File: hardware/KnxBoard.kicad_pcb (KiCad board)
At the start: 4 copper layers, 41.8 x 41.9 mm, 47 parts, among them IC0 STM32G491KEU6, IC1 NCN5130, J1 Conn_01x16, J2 Conn_01x16, J4 Conn_01x02_Male, X1 FA-238

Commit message: Routage OK need check and mass and texts
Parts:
- removed C1 (x2): 100 nF, Capacitor_SMD:C_0603_1608Metric_Pad1.08x0.95mm_HandSolder
- removed the C11 at (113.3, 55.4)
- removed C5_9: 100nF, Capacitor_SMD:C_0603_1608Metric_Pad1.08x0.95mm_HandSolder
- removed JP0, JP5: Bootloader, Jumper:SolderJumper-2_P1.3mm_Open_TrianglePad1.0x1.5mm
- added C20: 100 nF, Capacitor_SMD:C_0603_1608Metric_Pad1.08x0.95mm_HandSolder, F.Cu at (114.6, 36.1)
- added C8: 100nF 50V, Capacitor_SMD:C_0603_1608Metric_Pad1.08x0.95mm_HandSolder, F.Cu at (106.9, 61.2)
- added C9: 100uF 35V, Capacitor_SMD:CP_Elec_6.3x7.7, F.Cu at (92.2, 65.8)
- added JP3: Speed, Jumper:SolderJumper-3_P1.3mm_Open_RoundedPad1.0x1.5mm, B.Cu at (106.4, 49.0)
- added TP1: KNX_RXD, TestPoint:TestPoint_Pad_D1.0mm, F.Cu at (101.6, 50.0)
- added TP2: KNX_TXD, TestPoint:TestPoint_Pad_D1.0mm, F.Cu at (107.4, 47.8)
- C10: renamed from C12; value 1uF 35V ESR < 2ohm -> 1uF 50V ESR < 2ohm; moved to F.Cu
- C11: renamed from C19; moved to F.Cu
- C12: renamed from C20; moved to F.Cu
- C16, C17, C4: moved to F.Cu
- C21: renamed from C5; moved to F.Cu
- C22: renamed from C3; moved to F.Cu
- C23: renamed from C2; moved to F.Cu
- C24: renamed from C4; moved to F.Cu
- C3: renamed from C15; moved to F.Cu
- C4: renamed from C6; moved to F.Cu
- C5: renamed from C14; moved to F.Cu
- C6: renamed from C13; moved to F.Cu
- C7: renamed from C10; moved to F.Cu
- D1: value SS16 -> SS16T3G
- J1, J2: value Conn_01x16 -> Conn_01x15; footprint Connector_PinHeader_2.54mm:PinHeader_1x16_P2.54mm_Vertical -> Connector_PinHeader_2.54mm:PinHeader_1x15_P2.54mm_Vertical
- J4: value Conn_01x02_Male -> Conn_01x02
- JP1: value Bootflash -> Clock_8_16; footprint Jumper:SolderJumper-2_P1.3mm_Open_TrianglePad1.0x1.5mm -> Jumper:SolderJumper-3_P1.3mm_Open_RoundedPad1.0x1.5mm
- JP2: value RESETB_NRST -> Parity; footprint Jumper:SolderJumper-2_P1.3mm_Open_TrianglePad1.0x1.5mm -> Jumper:SolderJumper-3_P1.3mm_Open_RoundedPad1.0x1.5mm
- JP4: value Bootflash -> BootMode; footprint Jumper:SolderJumper-2_P1.3mm_Open_TrianglePad1.0x1.5mm -> Jumper:SolderJumper-3_P1.3mm_Open_RoundedPad1.0x1.5mm
- R22: renamed from R3; moved to F.Cu
- R3: renamed from R1; moved to B.Cu
- moved C11 21.5 mm to (113.3, 64.0), turned to 0 degrees
- moved JP4 21.0 mm to (112.5, 49.0), turned to 90 degrees
- moved R10 17.3 mm to (97.5, 65.3), turned to 0 degrees
- moved R18 16.4 mm to (109.7, 61.0), turned to -90 degrees
- moved C3 16.4 mm to (96.9, 61.7), turned to 0 degrees
- moved JP2 15.5 mm to (102.9, 49.0), turned to 90 degrees
- moved L2 15.1 mm to (109.2, 56.9)
- moved C4 14.1 mm to (97.5, 50.8), turned to -90 degrees
- moved R3 13.0 mm to (97.5, 65.0), turned to -90 degrees
- moved R21 12.5 mm to (113.8, 53.1), turned to 90 degrees
- moved JP1 12.3 mm to (99.6, 49.0), turned to 90 degrees
- moved C10 11.2 mm to (106.2, 64.0), turned to -90 degrees
- moved LD1 11.1 mm to (92.5, 49.3), turned to 180 degrees
- moved R30 11.1 mm to (92.5, 47.5)
- moved D1 10.9 mm to (109.2, 66.3)
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- renumbered C18 to C30, JP3 to JP7, L1 to L2, L2 to L3, R6 to R10, R2 to R18, R4 to R20, R5 to R21, R21 to R30
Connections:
- C10 pad 1: /KNXIFACE/Vfilt -> Net-(C10-Pad1)
- C4 pad 1: VDD -> +3V3
- D2 pad 1: /KNXIFACE/KNX+ -> GNDREF
- D2 pad 2: GNDREF -> /KNXIFACE/KNX+
- IC0 pad 19: KNX_RXD -> /KNXIFACE/KNX_RXD
- IC0 pad 20: KNX_TXD -> /KNXIFACE/KNX_TXD
- IC1 pad 10: /KNXIFACE/Vfilt -> Net-(C10-Pad1)
- IC1 pad 26: GNDREF -> Net-(IC1-Pad26)
- IC1 pad 27: KNX_RXD -> /KNXIFACE/KNX_RXD
- IC1 pad 28: KNX_TXD -> /KNXIFACE/KNX_TXD
- IC1 pad 29: GNDREF -> Net-(IC1-Pad29)
- IC1 pad 33: GNDREF -> Net-(JP1-Pad2)
- J1 pad 1: Prog -> +12V
- J1 pad 10: /MCU/PB4 -> /MCU/PB5
- J1 pad 11: /MCU/PB5 -> /MCU/PB6
- J1 pad 12: /MCU/PB6 -> /MCU/PB7
- J1 pad 13: /MCU/PB7 -> /MCU/PB8
- J1 pad 14: /MCU/PB8 -> VDD
- J1 pad 15: VDD -> GNDREF
- J1 pad 2: KNX_TXD -> GNDREF
- J1 pad 3: KNX_RXD -> unconnected-(J1-Pad3)
- J1 pad 4: KNX_RESETB -> NRST
- J1 pad 5: KNX_SAVEB -> /MCU/DEBUG_JTMS-SWDIO
- J1 pad 6: /MCU/DEBUG_JTMS-SWDIO -> /MCU/DEBUG_JTCK-SWCLK
- J1 pad 7: /MCU/DEBUG_JTCK-SWCLK -> /MCU/DEBUG_JTDI
- J1 pad 8: /MCU/DEBUG_JTDI -> /MCU/DEBUG_JTDA-SWO
- J1 pad 9: /MCU/DEBUG_JTDA-SWO -> /MCU/PB4
- J2 pad 1: +12V -> unconnected-(J2-Pad1)
- J2 pad 14: NRST -> /MCU/PF1
- J2 pad 15: /MCU/PF1 -> CLK16
- J2 pad 4: GNDREF -> Prog
- J4 pad 1: /KNXIFACE/KNX+ -> GNDREF
- J4 pad 2: GNDREF -> /KNXIFACE/KNX+
- JP1 pad 2: Net-(JP0-Pad1) -> Net-(JP1-Pad2)
- JP2 pad 1: NRST -> GNDREF
- JP2 pad 2: KNX_RESETB -> Net-(IC1-Pad29)
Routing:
- net GNDREF: track 0.00 -> 264.3 mm, vias 0 -> 34
- net VDD: track 0.00 -> 98.8 mm, vias 0 -> 4
- net Prog: track 0.00 -> 66.0 mm, vias 0 -> 2
- net CLK16: track 0.00 -> 65.1 mm, vias 0 -> 1
- net NRST: track 0.00 -> 53.9 mm, vias 0 -> 5
- net +3V3: track 0.00 -> 51.8 mm, vias 0 -> 4
- net /MCU/PA7: track 0.00 -> 33.5 mm, vias 0 -> 2
- net KNX_RESETB: track 0.00 -> 33.0 mm, vias 0 -> 2
- net /MCU/PA6: track 0.00 -> 32.5 mm, vias 0 -> 1
- net KNX_SAVEB: track 0.00 -> 32.0 mm, vias 0 -> 2
- net /MCU/PA5: track 0.00 -> 31.9 mm, vias 0 -> 1
- net Led: track 0.00 -> 30.7 mm, vias 0 -> 3
- net /MCU/DEBUG_JTMS-SWDIO: track 0.00 -> 28.2 mm
- net /MCU/PA4: track 0.00 -> 27.9 mm
- net +12V: track 0.00 -> 27.4 mm, vias 0 -> 2
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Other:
- board size 41.8 x 41.9 mm -> 38 x 39.9 mm

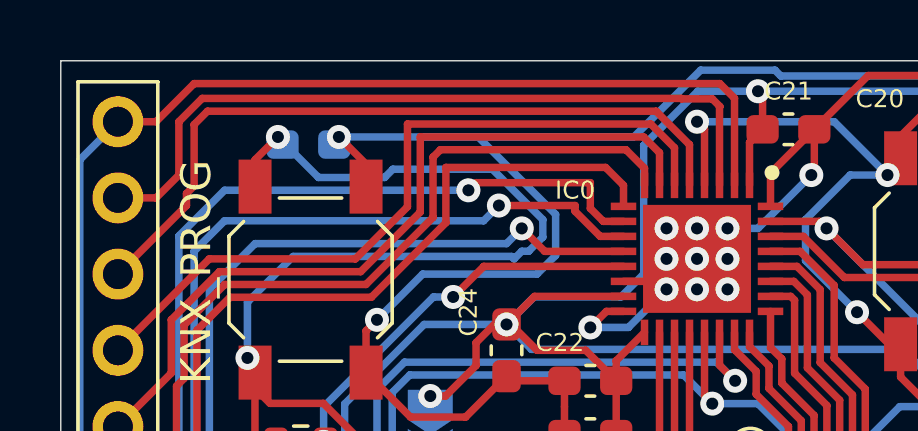
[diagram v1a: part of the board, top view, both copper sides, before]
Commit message: Chnage C10 side
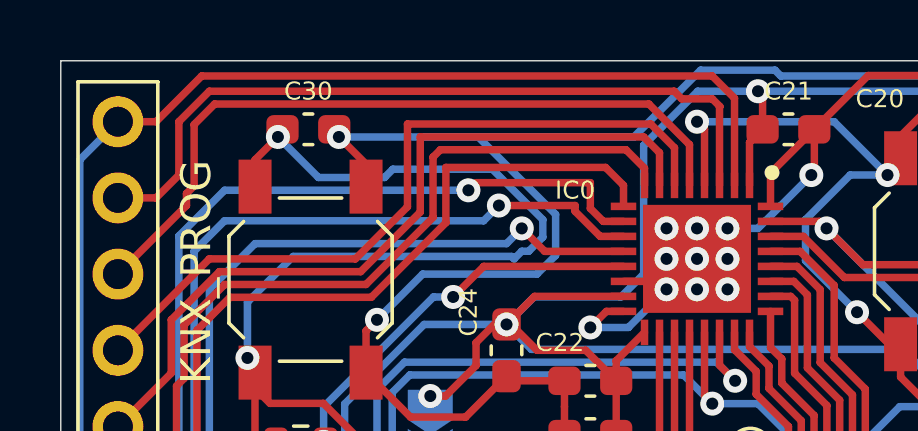
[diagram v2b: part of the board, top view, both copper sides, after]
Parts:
- C30: moved to F.Cu
- moved C30 0.51 mm to (92.7, 37.1)

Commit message: Seed SeeedStudio N°1
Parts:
- moved R3 7.37 mm to (90.2, 64.8)
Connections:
- net /MCU/DEBUG_JTDA-SWO renamed /MCU/PB3
- net /MCU/DEBUG_JTDI renamed /MCU/PA15
- net NRST renamed /MCU/NRST
- IC1 pad 21: +3V3 -> Net-(IC1-Pad21)
- IC1 pad 33: Net-(JP1-Pad2) -> unconnected-(IC1-Pad33)
- J1 pad 3: unconnected-(J1-Pad3) -> GNDREF
- J2 pad 1: unconnected-(J2-Pad1) -> GNDREF
- JP1 pad 2: Net-(JP1-Pad2) -> Net-(IC1-Pad21)
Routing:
- net Net-(IC1-Pad21): track 0.00 -> 17.5 mm, vias 0 -> 1
- net Net-(JP1-Pad2): track 10.5 -> 0.00 mm, vias 1 -> 0
- net +3V3: track 51.8 -> 45.8 mm
- net Net-(IC1-Pad38): track 8.01 -> 12.6 mm
- net +12V: track 27.4 -> 23.6 mm
- net GNDREF: track 264.3 -> 265.8 mm, vias 34 -> 35
- net /MCU/PA0: track 24.8 -> 23.7 mm
- net Net-(IC1-Pad20): track 11.2 -> 12.2 mm
- net /MCU/PF1: track 25.4 -> 24.5 mm
- net CLK16: track 65.3 -> 64.4 mm
- net /KNXIFACE/Vfilt: track 27.1 -> 26.5 mm
- added copper zone on B.Cu, net GNDREF
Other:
- outline, holes or cut-outs redrawn
- copper layers 4 -> 2
- board text added: "12V"
- board text added: "CLK16"
- board text added: "Fabien"
- board text added: "GND"
- board text added: "JP1: XCLKC 8MHz@GND 16MHz@VDD"
- board text added: "JP2: UART 9bit@GND 8bit@VDD"
- board text added: "JP3: UC1: 19200@GND 38400@VDD"
- board text added: "JP4: NC: BOOT0 or PB8"
- board text added: "JP6: RESETB to NRST"
- board text added: "JP7: PWR KNX to MCU"
- board text added: "KnxBoard"
- board text added: "LED"
- board text added: "NRST"
- board text added: "PA0"
- board text added: "PA1"
- board text added: "PA15"
- board text added: "PA4"
- board text added: "PA5"
- board text added: "PA6"
- board text added: "PA7"
- board text added: "PB3"
- board text added: "PB4"
- board text added: "PB5"
- board text added: "PB6"
- board text added: "PB7"
- board text added: "PB8"
- board text added: "PF1"
- board text added: "PROG"
- board text added: "Proriol"
- board text added: "RX"
- board text added: "SWCLK"
- board text added: "SWIO"
- board text added: "TX"
- board text added: "V4.0"
- board text added: "VDD"
